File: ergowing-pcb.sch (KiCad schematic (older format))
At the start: 16 parts, among them J1 USB_mini_micro_B, SW1 SW_PUSH, U1 ATMEGA32U4, X1 XTAL_GND

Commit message: Associate components and footprints
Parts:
- C1, C2, C3, C4, C5, C6, C7, C8: footprint (none) -> Capacitors_SMD:C_0805_HandSoldering
- J1: footprint (none) -> keyboard_parts:USB_miniB_hirose_5S8
- R1, R2, R3, R4: footprint (none) -> Resistors_SMD:R_0805_HandSoldering
- SW1: footprint (none) -> Buttons_Switches_SMD:SW_SPST_TL3342
- U1: footprint (none) -> Housings_QFP:TQFP-44_10x10mm_Pitch0.8mm
- X1: footprint (none) -> Crystals_Oscillators_SMD:crystal_FA238-TSX3225
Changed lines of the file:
@@
 F 0 "U1" H 3500 2450 60  0000 C CNN
 F 1 "ATMEGA32U4" H 3500 4950 60  0000 C CNN
-F 2 "" H 3500 3700 60  0000 C CNN
+F 2 "Housings_QFP:TQFP-44_10x10mm_Pitch0.8mm" H 3500 3700 60  0001 C CNN
 F 3 "" H 3500 3700 60  0000 C CNN
 	1    3500 3700
@@
 F 0 "X1" H 1150 4500 60  0000 C CNN
 F 1 "XTAL_GND" H 1150 4200 60  0000 C CNN
-F 2 "" H 1150 4350 60  0000 C CNN
+F 2 "Crystals_Oscillators_SMD:crystal_FA238-TSX3225" H 1150 4350 60  0001 C CNN
 F 3 "" H 1150 4350 60  0000 C CNN
 	1    1150 4350
@@
 F 0 "C1" H 760 4620 50  0000 L CNN
 F 1 "22p" H 760 4470 50  0000 L CNN
-F 2 "" H 750 4550 50  0001 C CNN
+F 2 "Capacitors_SMD:C_0805_HandSoldering" H 750 4550 50  0001 C CNN
 F 3 "" H 750 4550 50  0001 C CNN
 	1    750  4550
@@
 F 0 "C2" H 1560 4620 50  0000 L CNN
 F 1 "22p" H 1560 4470 50  0000 L CNN
-F 2 "" H 1550 4550 50  0001 C CNN
+F 2 "Capacitors_SMD:C_0805_HandSoldering" H 1550 4550 50  0001 C CNN
 F 3 "" H 1550 4550 50  0001 C CNN
 	1    1550 4550
@@
 $EndComp
 $Comp
-L GND #PWR?
+L GND #PWR01
 U 1 1 5B0804BD
 P 1150 4750
-F 0 "#PWR?" H 1150 4500 50  0001 C CNN
+F 0 "#PWR01" H 1150 4500 50  0001 C CNN
 F 1 "GND" H 1150 4600 50  0000 C CNN
 F 2 "" H 1150 4750 50  0001 C CNN
@@
 F 0 "C3" H 2960 1670 50  0000 L CNN
 F 1 "0.1u" H 2960 1520 50  0000 L CNN
-F 2 "" H 2950 1600 50  0001 C CNN
+F 2 "Capacitors_SMD:C_0805_HandSoldering" H 2950 1600 50  0001 C CNN
 F 3 "" H 2950 1600 50  0001 C CNN
 	1    2950 1600
@@
 F 0 "C4" H 3210 1670 50  0000 L CNN
 F 1 "0.1u" H 3210 1520 50  0000 L CNN
-F 2 "" H 3200 1600 50  0001 C CNN
+F 2 "Capacitors_SMD:C_0805_HandSoldering" H 3200 1600 50  0001 C CNN
 F 3 "" H 3200 1600 50  0001 C CNN
 	1    3200 1600
@@
 F 0 "C5" H 3460 1670 50  0000 L CNN
 F 1 "0.1u" H 3460 1520 50  0000 L CNN
-F 2 "" H 3450 1600 50  0001 C CNN
+F 2 "Capacitors_SMD:C_0805_HandSoldering" H 3450 1600 50  0001 C CNN
 F 3 "" H 3450 1600 50  0001 C CNN
 	1    3450 1600
@@
 F 0 "C6" H 3710 1670 50  0000 L CNN
 F 1 "0.1u" H 3710 1520 50  0000 L CNN
-F 2 "" H 3700 1600 50  0001 C CNN
+F 2 "Capacitors_SMD:C_0805_HandSoldering" H 3700 1600 50  0001 C CNN
 F 3 "" H 3700 1600 50  0001 C CNN
 	1    3700 1600
@@
 F 0 "C7" H 3960 1670 50  0000 L CNN
 F 1 "4.7u" H 3960 1520 50  0000 L CNN
-F 2 "" H 3950 1600 50  0001 C CNN
+F 2 "Capacitors_SMD:C_0805_HandSoldering" H 3950 1600 50  0001 C CNN
 F 3 "" H 3950 1600 50  0001 C CNN
 	1    3950 1600
@@
 $EndComp
 $Comp
-L GND #PWR?
+L GND #PWR02
 U 1 1 5B080C59
 P 2950 1900
-F 0 "#PWR?" H 2950 1650 50  0001 C CNN
+F 0 "#PWR02" H 2950 1650 50  0001 C CNN
 F 1 "GND" H 2950 1750 50  0000 C CNN
 F 2 "" H 2950 1900 50  0001 C CNN
@@
 $EndComp
 $Comp
-L VCC #PWR?
+L VCC #PWR03
 U 1 1 5B080C78
 P 2950 1300
-F 0 "#PWR?" H 2950 1150 50  0001 C CNN
+F 0 "#PWR03" H 2950 1150 50  0001 C CNN
 F 1 "VCC" H 2950 1450 50  0000 C CNN
 F 2 "" H 2950 1300 50  0001 C CNN
@@
 F 0 "SW1" H 1300 3960 50  0000 C CNN
 F 1 "SW_PUSH" H 1150 3770 50  0000 C CNN
-F 2 "" H 1150 3850 60  0000 C CNN
+F 2 "Buttons_Switches_SMD:SW_SPST_TL3342" H 1150 3850 60  0001 C CNN
 F 3 "" H 1150 3850 60  0000 C CNN
 	1    1150 3850
@@
 F 0 "R1" V 1280 3650 50  0000 C CNN
 F 1 "10K" V 1200 3650 50  0000 C CNN
-F 2 "" H 1200 3650 60  0000 C CNN
+F 2 "Resistors_SMD:R_0805_HandSoldering" H 1200 3650 60  0001 C CNN
 F 3 "" H 1200 3650 60  0000 C CNN
 	1    1200 3650
@@
 $EndComp
 $Comp
-L GND #PWR?
+L GND #PWR04
 U 1 1 5B0811C5
 P 750 3850
-F 0 "#PWR?" H 750 3600 50  0001 C CNN
+F 0 "#PWR04" H 750 3600 50  0001 C CNN
 F 1 "GND" H 750 3700 50  0000 C CNN
 F 2 "" H 750 3850 50  0001 C CNN
@@
 $EndComp
 $Comp
-L VCC #PWR?
+L VCC #PWR05
 U 1 1 5B0812B7
 P 850 3650
-F 0 "#PWR?" H 850 3500 50  0001 C CNN
+F 0 "#PWR05" H 850 3500 50  0001 C CNN
 F 1 "VCC" H 850 3800 50  0000 C CNN
 F 2 "" H 850 3650 50  0001 C CNN
@@
 F 0 "R2" V 5130 3750 50  0000 C CNN
 F 1 "10K" V 5050 3750 50  0000 C CNN
-F 2 "" H 5050 3750 60  0000 C CNN
+F 2 "Resistors_SMD:R_0805_HandSoldering" H 5050 3750 60  0001 C CNN
 F 3 "" H 5050 3750 60  0000 C CNN
 	1    5050 3750
@@
 $EndComp
 $Comp
-L GND #PWR?
+L GND #PWR06
 U 1 1 5B081BA9
 P 4850 4750
-F 0 "#PWR?" H 4850 4500 50  0001 C CNN
+F 0 "#PWR06" H 4850 4500 50  0001 C CNN
 F 1 "GND" H 4850 4600 50  0000 C CNN
 F 2 "" H 4850 4750 50  0001 C CNN
@@
 F 0 "J1" H 950 2850 60  0000 C CNN
 F 1 "USB_mini_micro_B" H 1200 3150 60  0001 C CNN
-F 2 "" H 1300 2900 60  0000 C CNN
+F 2 "keyboard_parts:USB_miniB_hirose_5S8" H 1300 2900 60  0001 C CNN
 F 3 "" H 1300 2900 60  0000 C CNN
 	1    1350 2900
@@
 F 0 "R3" V 2100 2950 50  0000 C CNN
 F 1 "22" V 2100 2750 50  0000 C CNN
-F 2 "" H 2100 2850 60  0000 C CNN
+F 2 "Resistors_SMD:R_0805_HandSoldering" H 2100 2850 60  0001 C CNN
 F 3 "" H 2100 2850 60  0000 C CNN
 	1    2100 2850
@@
 F 0 "R4" V 2100 3050 50  0000 C CNN
 F 1 "22" V 2100 2850 50  0000 C CNN
-F 2 "" H 2100 2950 60  0000 C CNN
+F 2 "Resistors_SMD:R_0805_HandSoldering" H 2100 2950 60  0001 C CNN
 F 3 "" H 2100 2950 60  0000 C CNN
 	1    2100 2950
@@
 F 0 "C8" V 2300 3200 50  0000 L CNN
 F 1 "1u" V 2300 3000 50  0000 L CNN
-F 2 "" H 2250 3150 50  0001 C CNN
+F 2 "Capacitors_SMD:C_0805_HandSoldering" H 2250 3150 50  0001 C CNN
 F 3 "" H 2250 3150 50  0001 C CNN
 	1    2250 3150
@@
 $EndComp
 $Comp
-L GND #PWR?
+L GND #PWR07
 U 1 1 5B083670
 P 1950 3050
-F 0 "#PWR?" H 1950 2800 50  0001 C CNN
+F 0 "#PWR07" H 1950 2800 50  0001 C CNN
 F 1 "GND" H 1950 2900 50  0000 C CNN
 F 2 "" H 1950 3050 50  0001 C CNN
@@
 $EndComp
 $Comp
-L VCC #PWR?
+L VCC #PWR08
 U 1 1 5B083DFD
 P 1600 2650
-F 0 "#PWR?" H 1600 2500 50  0001 C CNN
+F 0 "#PWR08" H 1600 2500 50  0001 C CNN
 F 1 "VCC" H 1600 2800 50  0000 C CNN
 F 2 "" H 1600 2650 50  0001 C CNN
@@
 $EndComp
 $Comp
-L VCC #PWR?
+L VCC #PWR09
 U 1 1 5B084385
 P 2050 3250
-F 0 "#PWR?" H 2050 3100 50  0001 C CNN
+F 0 "#PWR09" H 2050 3100 50  0001 C CNN
 F 1 "VCC" H 2050 3400 50  0000 C CNN
 F 2 "" H 2050 3250 50  0001 C CNN
@@
 $EndComp
 $Comp
-L VCC #PWR?
+L VCC #PWR010
 U 1 1 5B084453
 P 2350 3950
-F 0 "#PWR?" H 2350 3800 50  0001 C CNN
+F 0 "#PWR010" H 2350 3800 50  0001 C CNN
 F 1 "VCC" H 2350 4100 50  0000 C CNN
 F 2 "" H 2350 3950 50  0001 C CNN
@@
 $EndComp
 $Comp
-L GND #PWR?
+L GND #PWR011
 U 1 1 5B08448E
 P 2200 4050
-F 0 "#PWR?" H 2200 3800 50  0001 C CNN
+F 0 "#PWR011" H 2200 3800 50  0001 C CNN
 F 1 "GND" H 2200 3900 50  0000 C CNN
 F 2 "" H 2200 4050 50  0001 C CNN
@@
 $EndComp
 $Comp
-L VCC #PWR?
+L VCC #PWR012
 U 1 1 5B08551D
 P 4700 2650
-F 0 "#PWR?" H 4700 2500 50  0001 C CNN
+F 0 "#PWR012" H 4700 2500 50  0001 C CNN
 F 1 "VCC" H 4700 2800 50  0000 C CNN
 F 2 "" H 4700 2650 50  0001 C CNN
@@
 $EndComp
 $Comp
-L GND #PWR?
+L GND #PWR013
 U 1 1 5B085648
 P 4850 2750
-F 0 "#PWR?" H 4850 2500 50  0001 C CNN
+F 0 "#PWR013" H 4850 2500 50  0001 C CNN
 F 1 "GND" H 4850 2600 50  0000 C CNN
 F 2 "" H 4850 2750 50  0001 C CNN
@@
 $EndComp
 $Comp
-L GND #PWR?
+L GND #PWR014
 U 1 1 5B085683
 P 4850 3550
-F 0 "#PWR?" H 4850 3300 50  0001 C CNN
+F 0 "#PWR014" H 4850 3300 50  0001 C CNN
 F 1 "GND" H 4850 3400 50  0000 C CNN
 F 2 "" H 4850 3550 50  0001 C CNN
@@
 $EndComp
 $Comp
-L VCC #PWR?
+L VCC #PWR015
 U 1 1 5B0856BE
 P 4700 4650
-F 0 "#PWR?" H 4700 4500 50  0001 C CNN
+F 0 "#PWR015" H 4700 4500 50  0001 C CNN
 F 1 "VCC" H 4700 4800 50  0000 C CNN
 F 2 "" H 4700 4650 50  0001 C CNN
@@
 col13
 $Comp
-L VCC #PWR?
+L VCC #PWR016
 U 1 1 5B18ACEE
 P 4700 3650
-F 0 "#PWR?" H 4700 3500 50  0001 C CNN
+F 0 "#PWR016" H 4700 3500 50  0001 C CNN
 F 1 "VCC" H 4700 3800 50  0000 C CNN
 F 2 "" H 4700 3650 50  0001 C CNN
@@
 $EndComp
 $Comp
-L GND #PWR?
+L GND #PWR017
 U 1 1 5B18B237
 P 5400 3750
-F 0 "#PWR?" H 5400 3500 50  0001 C CNN
+F 0 "#PWR017" H 5400 3500 50  0001 C CNN
 F 1 "GND" H 5400 3600 50  0000 C CNN
 F 2 "" H 5400 3750 50  0001 C CNN

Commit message: Pre-messing around #1
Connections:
- net row1: now also U1.28 (PB4); no longer U1.31 (PC6)
- net row2: now also U1.29 (PB5); no longer U1.30 (PB6)
- net row3: now also U1.30 (PB6); no longer U1.29 (PB5)
- net row4: now also U1.31 (PC6); no longer U1.28 (PB4)
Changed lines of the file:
@@
 row0
 Text GLabel 4600 3950 2    60   Input ~ 0
+row4
+Text GLabel 4600 4050 2    60   Input ~ 0
+row3
+Text GLabel 4600 4150 2    60   Input ~ 0
+row2
+Text GLabel 4600 4250 2    60   Input ~ 0
 row1
-Text GLabel 4600 4050 2    60   Input ~ 0
-row2
-Text GLabel 4600 4150 2    60   Input ~ 0
-row3
-Text GLabel 4600 4250 2    60   Input ~ 0
-row4
 Text GLabel 2450 3650 0    60   Input ~ 0
 col0

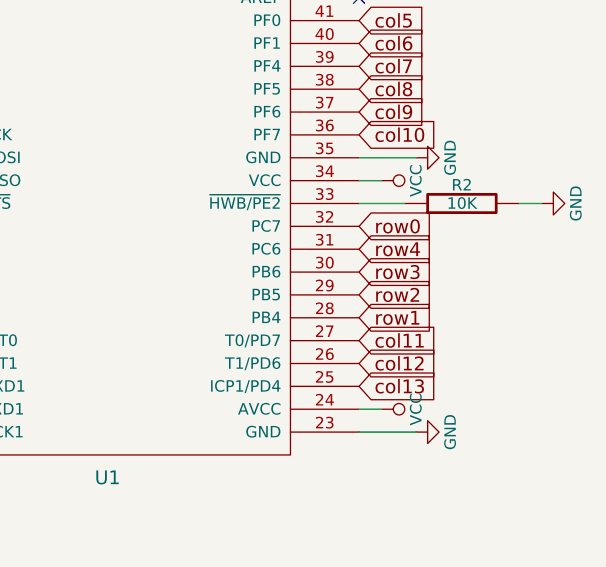
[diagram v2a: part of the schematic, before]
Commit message: Revert "Pre-messing around #1"
This reverts commit 32e58cf0b1eda56b39c79379dba13b735693d8cf.
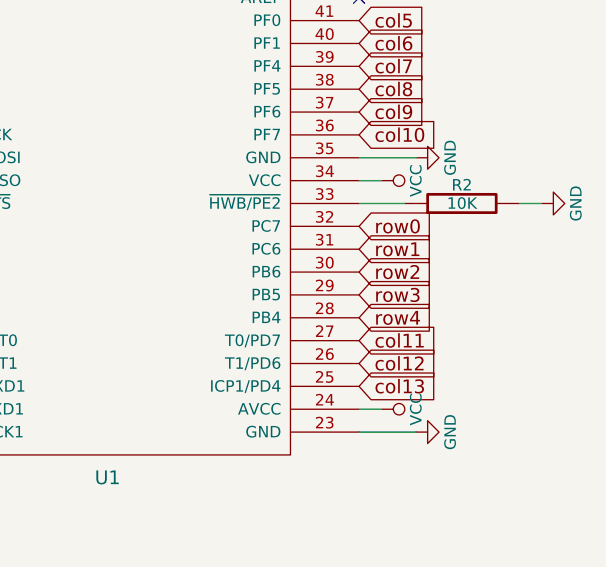
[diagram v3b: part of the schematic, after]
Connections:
- net row1: now also U1.31 (PC6); no longer U1.28 (PB4)
- net row2: now also U1.30 (PB6); no longer U1.29 (PB5)
- net row3: now also U1.29 (PB5); no longer U1.30 (PB6)
- net row4: now also U1.28 (PB4); no longer U1.31 (PC6)
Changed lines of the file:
@@
 row0
 Text GLabel 4600 3950 2    60   Input ~ 0
+row1
+Text GLabel 4600 4050 2    60   Input ~ 0
+row2
+Text GLabel 4600 4150 2    60   Input ~ 0
+row3
+Text GLabel 4600 4250 2    60   Input ~ 0
 row4
-Text GLabel 4600 4050 2    60   Input ~ 0
-row3
-Text GLabel 4600 4150 2    60   Input ~ 0
-row2
-Text GLabel 4600 4250 2    60   Input ~ 0
-row1
 Text GLabel 2450 3650 0    60   Input ~ 0
 col0
